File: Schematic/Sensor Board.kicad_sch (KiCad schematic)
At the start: 0 parts

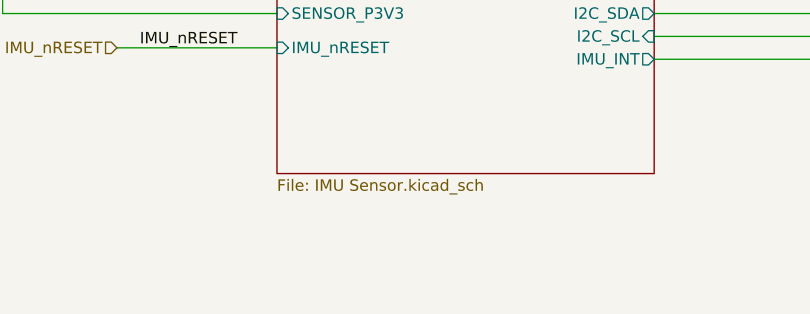
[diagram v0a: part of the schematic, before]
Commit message: updated fuel guage
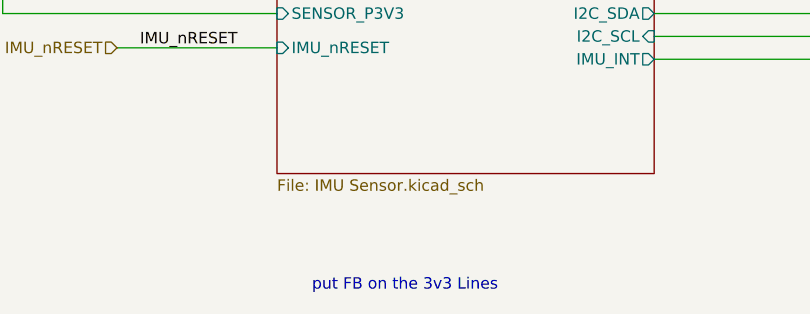
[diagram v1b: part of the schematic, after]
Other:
- note added: "put FB on the 3v3 Lines"
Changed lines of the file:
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@@
 	(generator_version "9.0")
 	(paper "A4")
+	(text "put FB on the 3v3 Lines"
+		(exclude_from_sim no)
+		(at 134.874 154.686 0)
+		(effects
+			(font
+				(size 1.27 1.27)
+			)
+		)
+	)
 	(junction
 		(at 90.17 90.17)

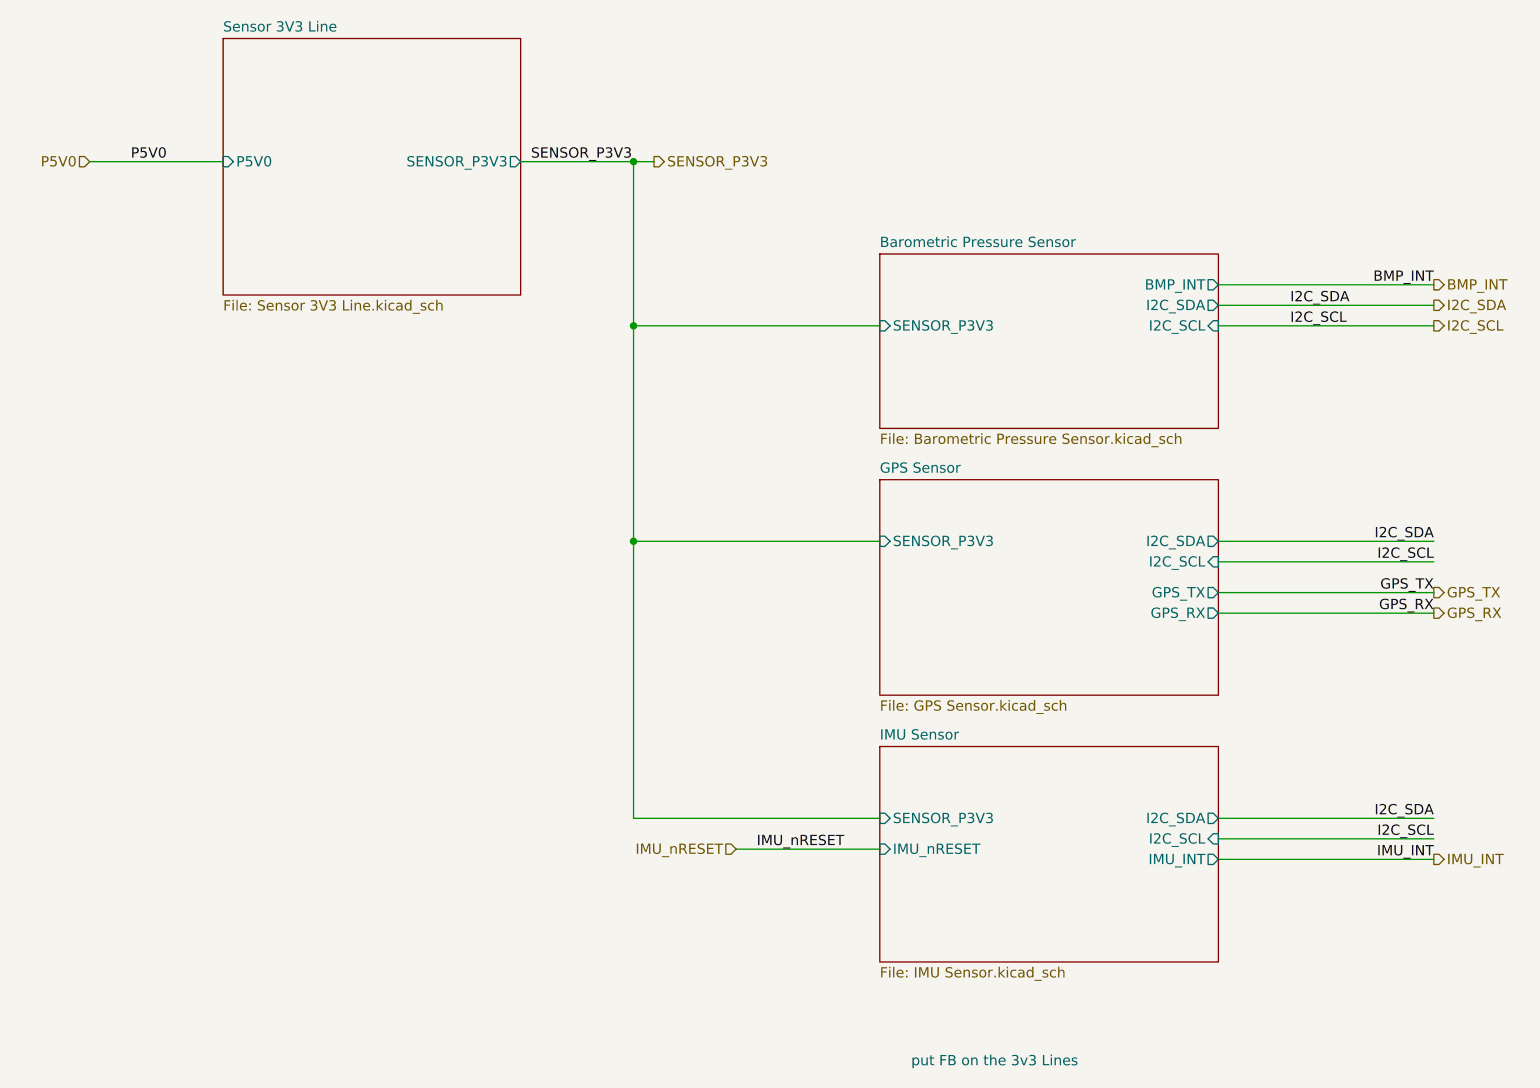
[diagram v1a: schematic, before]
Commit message: Added MCU
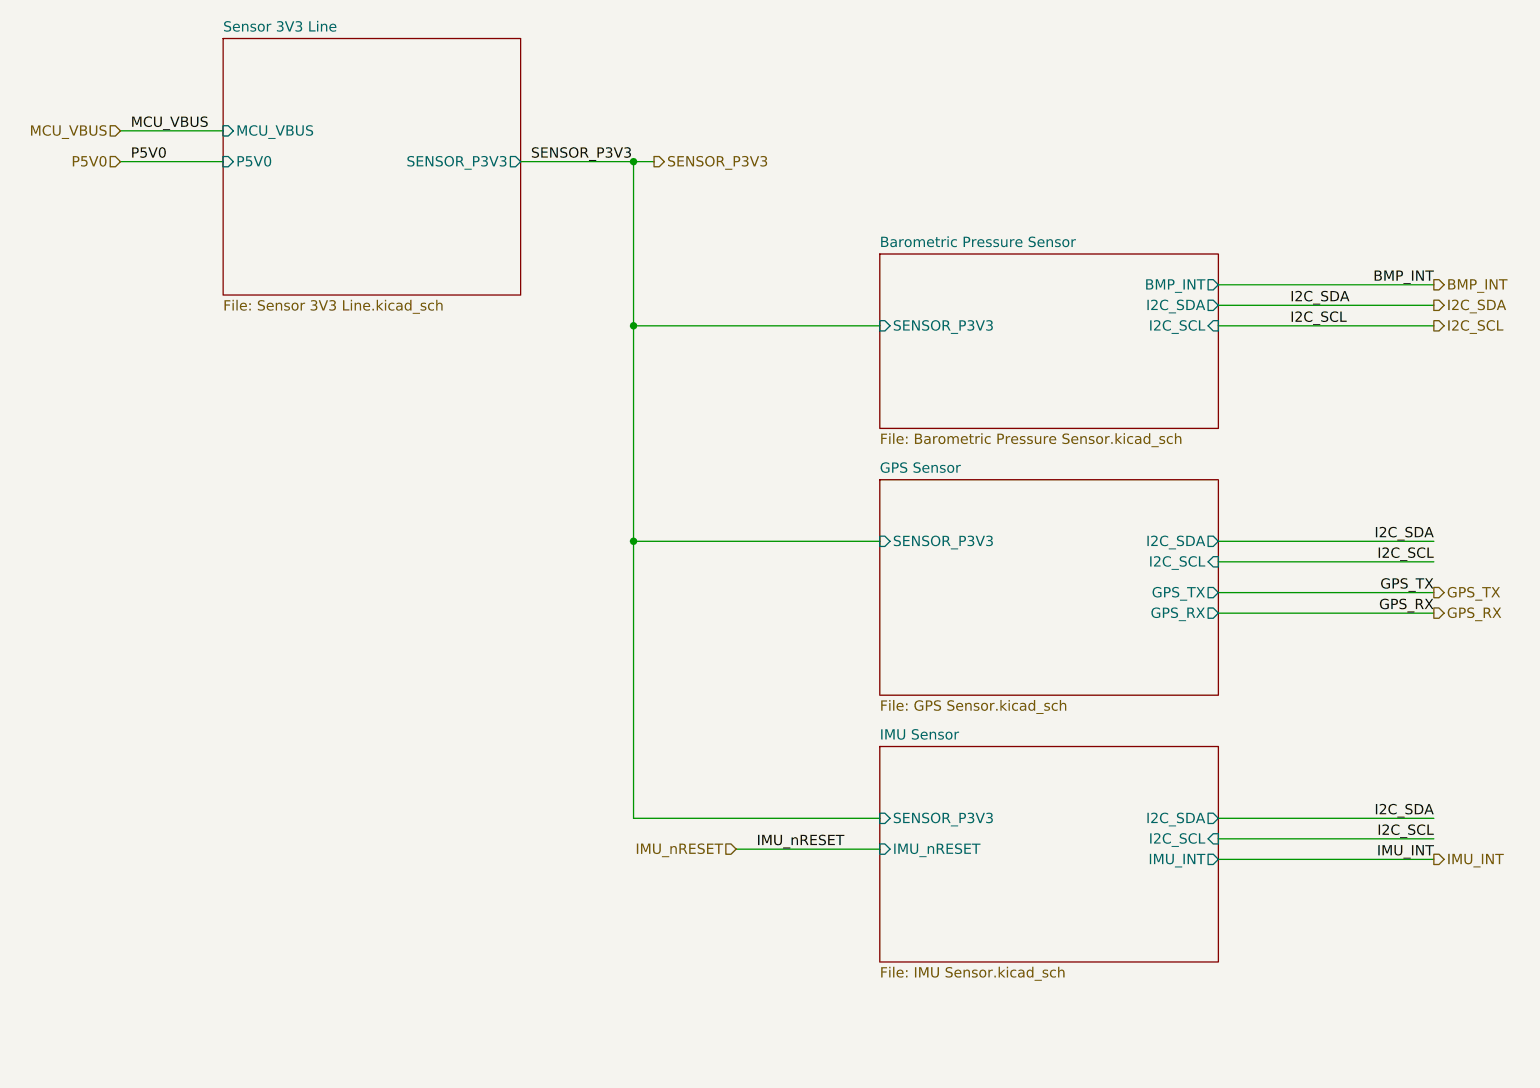
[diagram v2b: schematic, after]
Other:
- sheet Sensor 3V3 Line ports: added MCU_VBUS; removed none
- note removed: "put FB on the 3v3 Lines"
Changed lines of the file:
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@@
 	(generator_version "9.0")
 	(paper "A4")
-	(text "put FB on the 3v3 Lines"
-		(exclude_from_sim no)
-		(at 134.874 154.686 0)
-		(effects
-			(font
-				(size 1.27 1.27)
-			)
-		)
-	)
 	(junction
 		(at 90.17 90.17)
@@
 	(wire
 		(pts
-			(xy 22.86 43.18) (xy 39.37 43.18)
+			(xy 26.67 43.18) (xy 39.37 43.18)
 		)
 		(stroke
@@
 		(pts
 			(xy 162.56 96.52) (xy 189.23 96.52)
+		)
+		(stroke
+			(width 0)
+			(type default)
+		)
+	)
+	(wire
+		(pts
+			(xy 26.67 39.37) (xy 39.37 39.37)
 		)
 		(stroke
@@
 	(label "I2C_SDA"
 		(at 171.45 60.96 0)
+		(effects
+			(font
+				(size 1.27 1.27)
+			)
+			(justify left bottom)
+		)
+	)
+	(label "MCU_VBUS"
+		(at 27.94 39.37 0)
 		(effects
 			(font
@@
 	(hierarchical_label "P5V0"
 		(shape input)
-		(at 22.86 43.18 180)
+		(at 26.67 43.18 180)
+		(effects
+			(font
+				(size 1.27 1.27)
+			)
+			(justify right)
+		)
+	)
+	(hierarchical_label "MCU_VBUS"
+		(shape input)
+		(at 26.67 39.37 180)
 		(effects
 			(font
@@
 			(project "STAR"
 				(path "/fc8533bc-25dd-4c20-9b4c-ffebebd6739b/93231d0a-659f-4d39-8e8d-78b96a3896a1"
-					(page "30")
+					(page "37")
 				)
 			)
@@
 			(project "STAR"
 				(path "/fc8533bc-25dd-4c20-9b4c-ffebebd6739b/93231d0a-659f-4d39-8e8d-78b96a3896a1"
-					(page "32")
+					(page "39")
 				)
 			)
@@
 			)
 		)
+		(pin "MCU_VBUS" input
+			(at 39.37 39.37 180)
+			(effects
+				(font
+					(size 1.27 1.27)
+				)
+				(justify left)
+			)
+		)
 		(instances
 			(project "STAR"
 				(path "/fc8533bc-25dd-4c20-9b4c-ffebebd6739b/93231d0a-659f-4d39-8e8d-78b96a3896a1"
-					(page "23")
+					(page "36")
 				)
 			)
@@
 			(project "STAR"
 				(path "/fc8533bc-25dd-4c20-9b4c-ffebebd6739b/93231d0a-659f-4d39-8e8d-78b96a3896a1"
-					(page "31")
-				)
-			)
+					(page "38")
+				)
+			)

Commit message: Massive pivit, simplification
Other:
- removed sheet Barometric Pressure Sensor
- removed sheet GPS Sensor
- removed sheet IMU Sensor
